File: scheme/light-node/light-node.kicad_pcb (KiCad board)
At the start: 2 copper layers, 0 parts

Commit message: light-node: PCB done
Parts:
- added D1: LED, LED-3MM, F.Cu at (68.1, 48.8)
- added P1: CONN_2, bornier2, F.Cu at (30.7, 41.1)
- added P2: CONN_2, bornier2, F.Cu at (119.1, 41.1)
- added P3: CONN_6, PIN_ARRAY-6X1, F.Cu at (76.2, 44.7)
- added Q1: NPN, TO92-123, F.Cu at (80.0, 51.6)
- added R1: 10K, R1, F.Cu at (87.6, 25.9)
- added R2: 10K, R1, F.Cu at (51.8, 50.3)
- added R3: 10K, R1, F.Cu at (52.1, 47.0)
- added R4: 10K, R1, F.Cu at (87.1, 41.1)
- added R5: 10K, R1, F.Cu at (73.7, 52.8)
- added R6: 1K, R1, F.Cu at (73.7, 48.5)
- added R7: 10K, R1, F.Cu at (68.8, 52.8)
- added RL1: RZ03-1C4-D005, RELAY-2, F.Cu at (88.6, 44.2)
- added SW1: SW_RESET, SW_PUSH_SMALL, F.Cu at (60.2, 51.8)
- added SW2: SW_PROGRAM, SW_PUSH_SMALL, F.Cu at (43.4, 51.6)
- added T1: 220 VAC 5 VDC, Power_USB_hack, F.Cu at (61.0, 33.0)
- added U1: SPX2920M3-3.3, TO220_VERT_123, F.Cu at (60.2, 45.7)
- added U2: ESP866_ESP-12E, ESP8266-ESP-12E, F.Cu at (102.9, 32.8)
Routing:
- net /AC_N: track 0.00 -> 146.5 mm, vias 0 -> 1
- net /GND: track 0.00 -> 124.1 mm
- net /AC_L: track 0.00 -> 109.3 mm
- net N-0000018: track 0.00 -> 88.0 mm, vias 0 -> 2
- net N-0000016: track 0.00 -> 78.2 mm, vias 0 -> 3
- net /3.3Vcc: track 0.00 -> 78.0 mm
- net N-0000017: track 0.00 -> 70.3 mm, vias 0 -> 2
- net N-000002: track 0.00 -> 58.0 mm, vias 0 -> 2
- net /5Vcc: track 0.00 -> 50.8 mm, vias 0 -> 1
- net /ESP_RX: track 0.00 -> 48.6 mm, vias 0 -> 1
- net /RELAY: track 0.00 -> 43.7 mm, vias 0 -> 1
- net /ESP_TX: track 0.00 -> 33.6 mm, vias 0 -> 1
- net /LED: track 0.00 -> 30.5 mm, vias 0 -> 1
- net /AC_Lout: track 0.00 -> 17.7 mm
- net N-000003: track 0.00 -> 12.5 mm
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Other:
- board outline added: 95 x 36.8 mm
- board text added: "pgr"
- board text added: "rst"

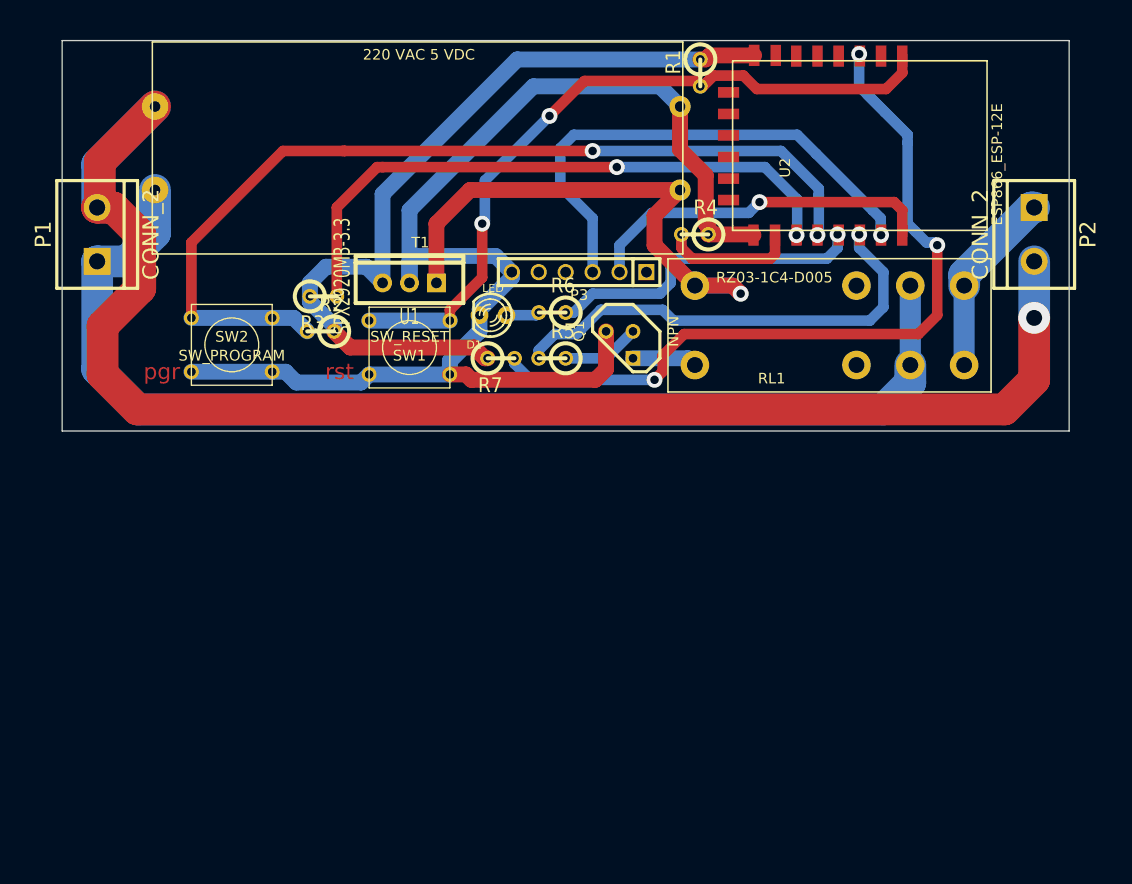
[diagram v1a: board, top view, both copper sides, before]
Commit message: pcb: version 2, with a hole for USB charger
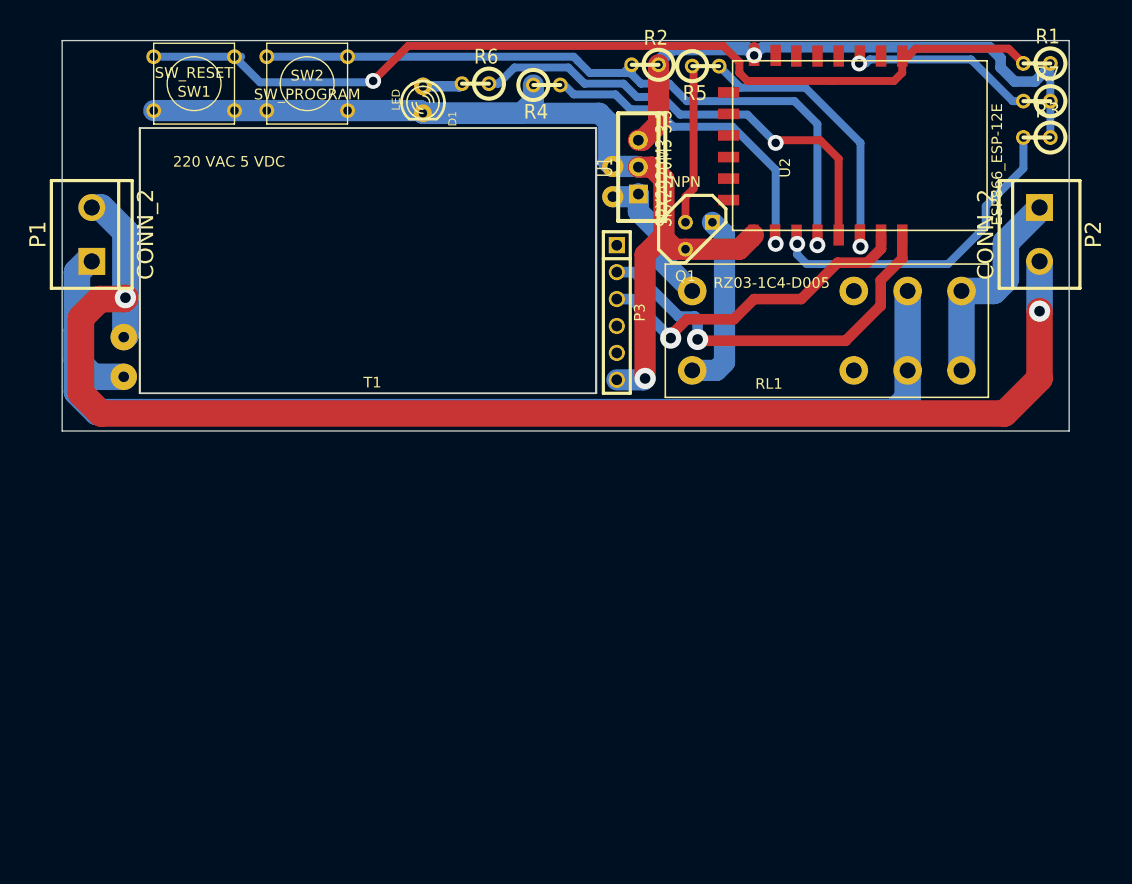
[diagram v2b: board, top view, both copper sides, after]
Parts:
- T1: footprint Power_USB_hack -> USB_Power_Hack_v2
- moved R3 69.0 mm to (119.4, 32.0), turned to 180 degrees
- moved R7 56.1 mm to (119.4, 28.6), turned to 180 degrees
- moved R2 39.6 mm to (82.4, 25.1)
- moved SW1 32.1 mm to (39.9, 26.9)
- moved R1 31.8 mm to (119.4, 25.0), turned to 180 degrees
- moved R5 31.1 mm to (88.1, 25.3), turned to 0 degrees
- moved SW2 25.6 mm to (50.5, 26.9)
- moved U1 24.2 mm to (81.8, 34.8), turned to 0 degrees
- moved R6 22.8 mm to (66.4, 26.9)
- moved D1 21.4 mm to (61.5, 28.4), turned to 270 degrees
- moved R4 19.8 mm to (73.2, 27.1), turned to 0 degrees
- moved T1 17.8 mm to (43.2, 34.3)
- moved Q1 12.7 mm to (87.5, 41.3), turned to 0 degrees
- moved P3 5.21 mm to (79.8, 48.5), turned to 270 degrees
- moved RL1 0.57 mm to (88.4, 44.7)
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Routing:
- net N-0000016: track 78.2 -> 18.0 mm, vias 3 -> 1
- net /5Vcc: track 50.8 -> 13.8 mm, vias 1 -> 0
- net /GND: track 124.1 -> 97.2 mm, vias 0 -> 1
- net N-000002: track 58.0 -> 31.3 mm, vias 2 -> 1
- net /3.3Vcc: track 78.0 -> 56.9 mm, vias 0 -> 1
- net N-0000017: track 70.3 -> 90.7 mm, vias 2 -> 1
- net N-000003: track 12.5 -> 31.5 mm, vias 0 -> 1
- net N-0000018: track 88.0 -> 70.0 mm, vias 2 -> 1
- net /ESP_RX: track 48.6 -> 31.4 mm
- net /AC_N: track 146.5 -> 129.8 mm, vias 1 -> 2
- net /RELAY: track 43.7 -> 27.2 mm
- net /LED: track 30.5 -> 44.6 mm
- net N-0000010: track 6.11 -> 17.0 mm
- net N-000009: track 7.40 -> 15.1 mm
- net /ESP_TX: track 33.6 -> 37.6 mm
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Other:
- outline, holes or cut-outs redrawn
- board text removed: "pgr"
- board text removed: "rst"

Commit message: light-node: upload last version
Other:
- board text added: "ARCO | 2016/02/10"
- board text added: "g"
- board text added: "g · · t r ·"
- board text added: "v"
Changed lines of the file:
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@@
     (area 23.9776 21.4249 125.8824 59.740001)
     (thickness 1.6)
-    (drawings 8)
+    (drawings 12)
     (tracks 218)
     (zones 0)
@@
     (15 F.Cu signal)
     (0 B.Cu signal)
-    (16 B.Adhes user)
-    (17 F.Adhes user)
-    (18 B.Paste user)
-    (19 F.Paste user)
-    (20 B.SilkS user)
+    (16 B.Adhes user hide)
+    (17 F.Adhes user hide)
+    (18 B.Paste user hide)
+    (19 F.Paste user hide)
+    (20 B.SilkS user hide)
     (21 F.SilkS user)
-    (22 B.Mask user)
-    (23 F.Mask user)
-    (24 Dwgs.User user)
-    (25 Cmts.User user)
-    (26 Eco1.User user)
+    (22 B.Mask user hide)
+    (23 F.Mask user hide)
+    (24 Dwgs.User user hide)
+    (25 Cmts.User user hide)
+    (26 Eco1.User user hide)
     (27 Eco2.User user)
     (28 Edge.Cuts user)
   )
   (setup
-    (last_trace_width 0.75)
+    (last_trace_width 0.254)
     (user_trace_width 0.75)
     (user_trace_width 1)
@@
     )
   )
+  (gr_text "g · · t r ·" (at 82.423 47.117 90) (layer F.SilkS)
+    (effects (font (size 1.5 1.5) (thickness 0.3)))
+  )
+  (gr_text "ARCO | 2016/02/10" (at 51.562 57.912) (layer F.SilkS)
+    (effects (font (size 1.5 1.5) (thickness 0.3)))
+  )
+  (gr_text v (at 78.867 39.624 270) (layer F.SilkS)
+    (effects (font (size 1.5 1.5) (thickness 0.3)))
+  )
+  (gr_text g (at 79.121 32.512 270) (layer F.SilkS)
+    (effects (font (size 1.5 1.5) (thickness 0.3)))
+  )
   (gr_line (start 77.851 31.115) (end 34.798 31.115) (angle 90) (layer Edge.Cuts) (width 0.1))

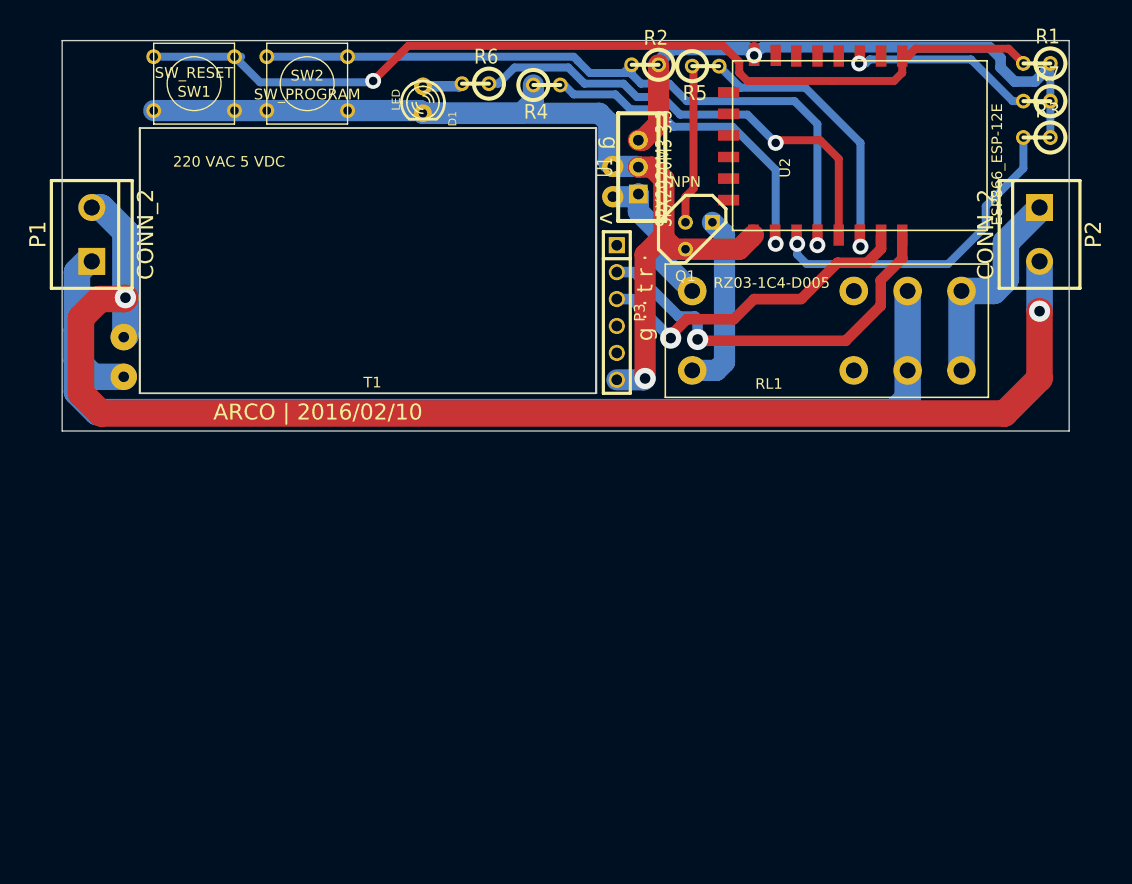
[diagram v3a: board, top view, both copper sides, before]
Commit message: light-node: panelized for dirtypcbs
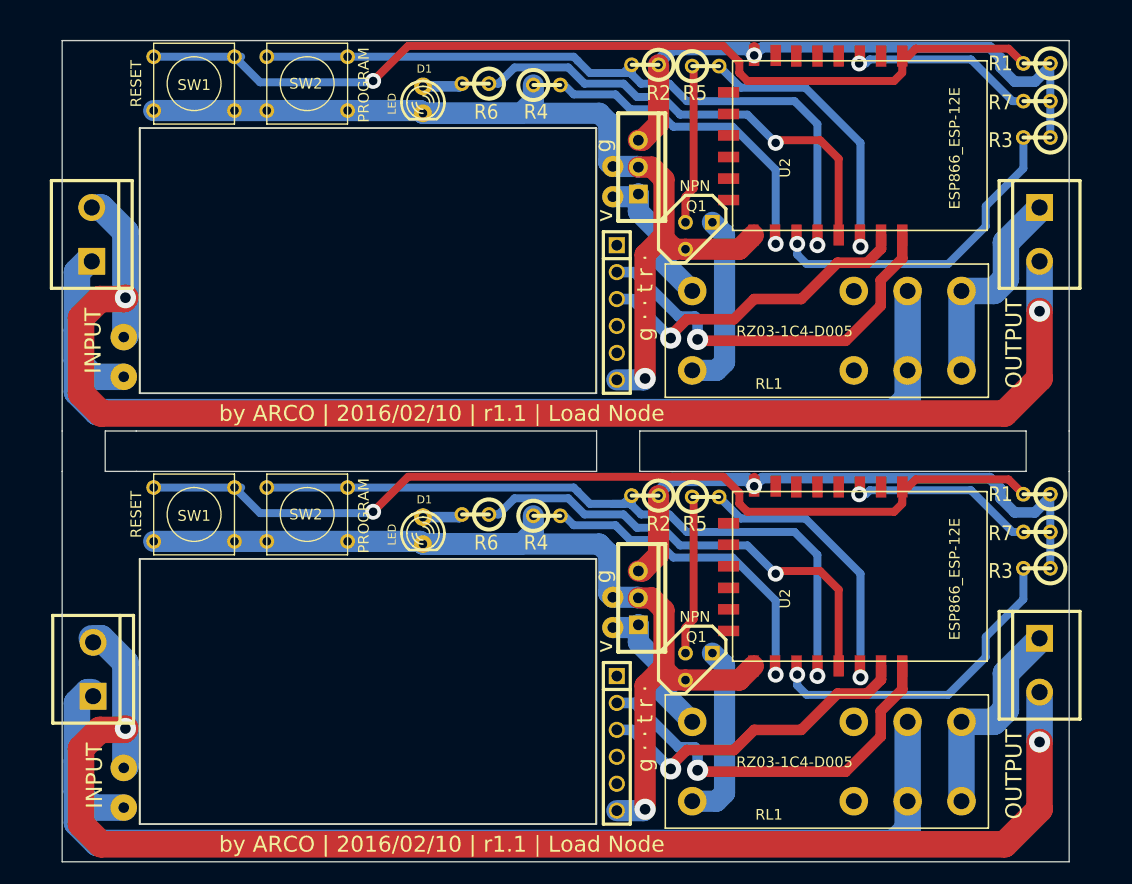
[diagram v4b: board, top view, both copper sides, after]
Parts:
- added D1: LED, LED-3MM, F.Cu at (61.5, 69.1)
- added P1: INPUT, bornier2, F.Cu at (30.4, 82.2)
- added P2: OUTPUT, bornier2, F.Cu at (119.6, 81.8)
- added P3: CONN_6, PIN_ARRAY-6X1, F.Cu at (79.8, 89.2)
- added Q1: NPN, TO92-123, F.Cu at (87.5, 81.9)
- added R1: 10K, R1, F.Cu at (119.4, 65.7)
- added R2: 10K, R1, F.Cu at (82.4, 65.8)
- added R3: 10K, R1, F.Cu at (119.4, 72.6)
- added R4: 10K, R1, F.Cu at (73.2, 67.7)
- added R5: 10K, R1, F.Cu at (88.1, 65.9)
- added R6: 1K, R1, F.Cu at (66.4, 67.6)
- added R7: 10K, R1, F.Cu at (119.4, 69.2)
- added RL1: RZ03-1C4-D005, RELAY-2, F.Cu at (88.4, 85.3)
- added SW1: RESET, SW_PUSH_SMALL, F.Cu at (39.9, 67.6)
- added SW2: PROGRAM, SW_PUSH_SMALL, F.Cu at (50.5, 67.6)
- added T1: 220 VAC 5 VDC, USB_Power_Hack_v2, F.Cu at (43.2, 74.9)
- added U1: SPX2920M3-3.3, TO220_VERT_123, F.Cu at (81.8, 75.4)
- added U2: ESP866_ESP-12E, ESP8266-ESP-12E, F.Cu at (102.9, 73.4)
- P1: value CONN_2 -> INPUT
- P2: value CONN_2 -> OUTPUT
- SW1: value SW_RESET -> RESET
- SW2: value SW_PROGRAM -> PROGRAM
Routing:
- net /AC_N: track 129.8 -> 259.7 mm, vias 2 -> 4
- net /AC_L: track 110.9 -> 221.8 mm
- net /GND: track 97.2 -> 194.5 mm, vias 1 -> 2
- net N-0000017: track 90.7 -> 181.3 mm, vias 1 -> 2
- net N-0000018: track 70.0 -> 140.0 mm, vias 1 -> 2
- net /3.3Vcc: track 56.9 -> 113.8 mm, vias 1 -> 2
- net /LED: track 44.6 -> 89.2 mm, vias 1 -> 2
- net /ESP_TX: track 37.6 -> 75.1 mm, vias 1 -> 2
- net N-000003: track 31.5 -> 62.9 mm, vias 1 -> 2
- net /ESP_RX: track 31.4 -> 62.8 mm, vias 1 -> 2
- net N-000002: track 31.3 -> 62.7 mm, vias 1 -> 2
- net /RELAY: track 27.2 -> 54.4 mm, vias 1 -> 2
- net /AC_Lout: track 20.2 -> 40.4 mm
- net N-0000016: track 18.0 -> 36.0 mm, vias 1 -> 2
- net N-0000010: track 17.0 -> 34.1 mm
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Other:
- board size 95 x 36.8 mm -> 95 x 77.5 mm
- board text added: "by ARCO | 2016/02/10 | r1.1 | Load Node"
- board text removed: "ARCO | 2016/02/10"
